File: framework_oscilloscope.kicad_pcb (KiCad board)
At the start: 4 copper layers, 26 x 44 mm, 83 parts, among them IC1 FT232HL-REEL, IC10 93LC56BT-I_OT, IC2 ICE40UP5K-SG48I, IC3 ADC08060CIMTX_NOPB, IC7 OPA356AIDBVR, IC8 TLV77312PDBVR, IC9 LM4040C20IDBZT, J1 BNC, P1 USB_C_Plug_USB2.0, U9 TPS62A02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

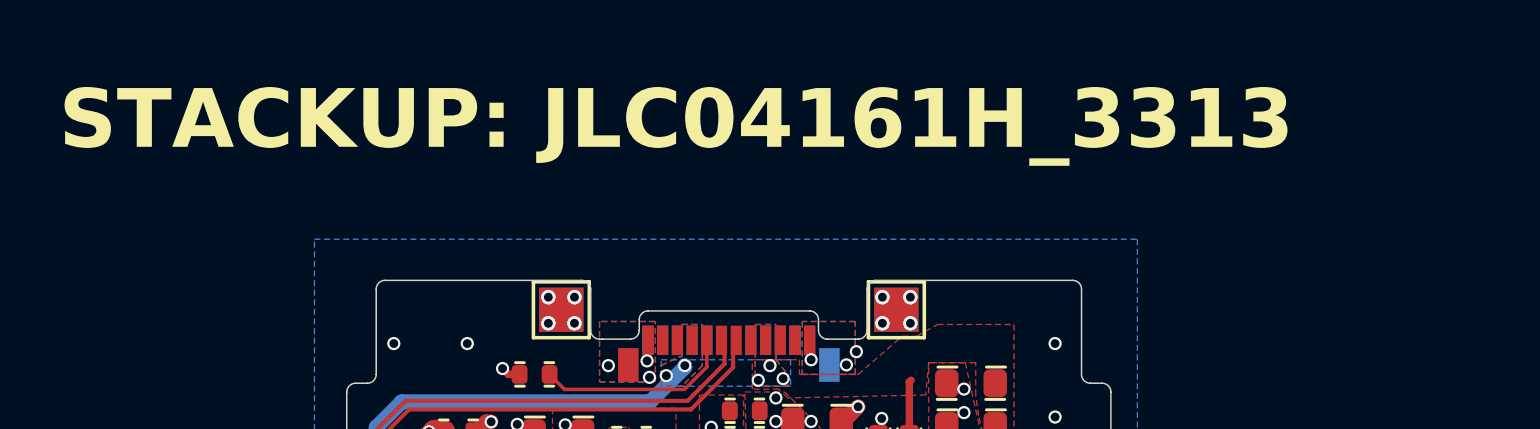
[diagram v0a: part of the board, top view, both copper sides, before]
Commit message: changed stackup name to a similar 0.8mm one
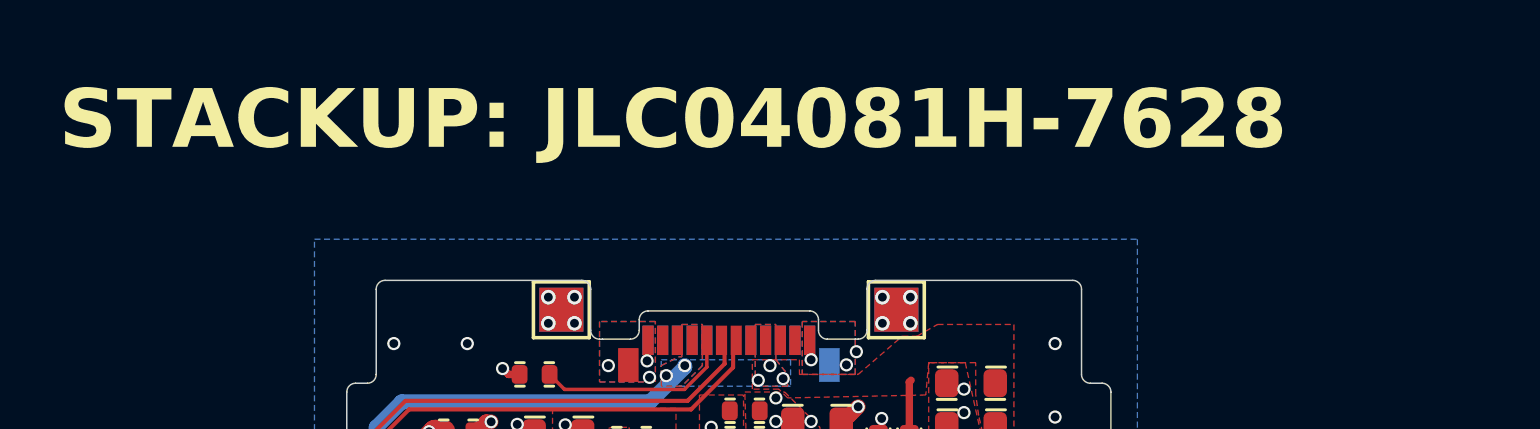
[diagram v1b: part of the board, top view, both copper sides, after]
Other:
- board text added: "STACKUP: JLC04081H-7628"
- board text removed: "STACKUP: JLC04161H_3313"
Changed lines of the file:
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@@
 		(layer "Edge.Cuts")
 	)
-	(gr_text "STACKUP: JLC04161H_3313"
+	(gr_text "STACKUP: JLC04081H-7628"
 		(at 45.45 31.725 0)
 		(layer "F.SilkS")

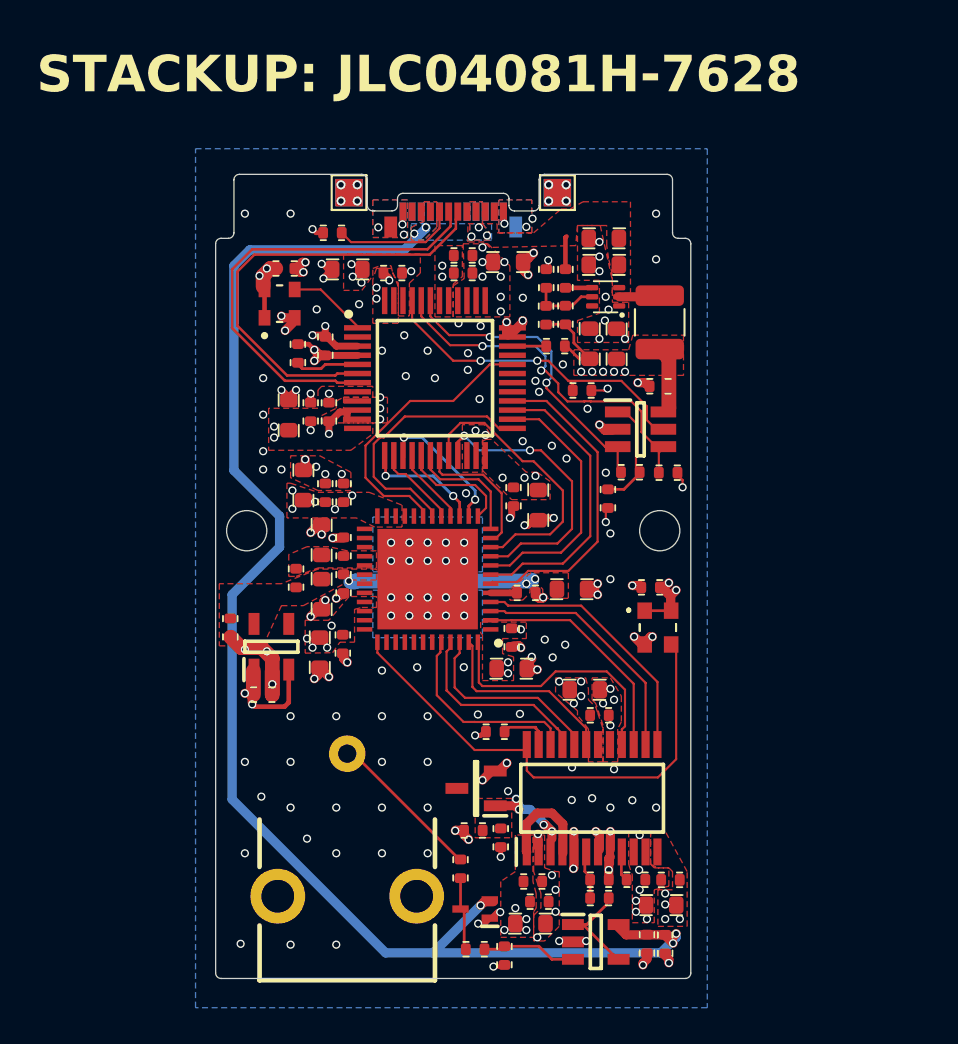
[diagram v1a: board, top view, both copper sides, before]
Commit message: fixed FT232-FPGA connections
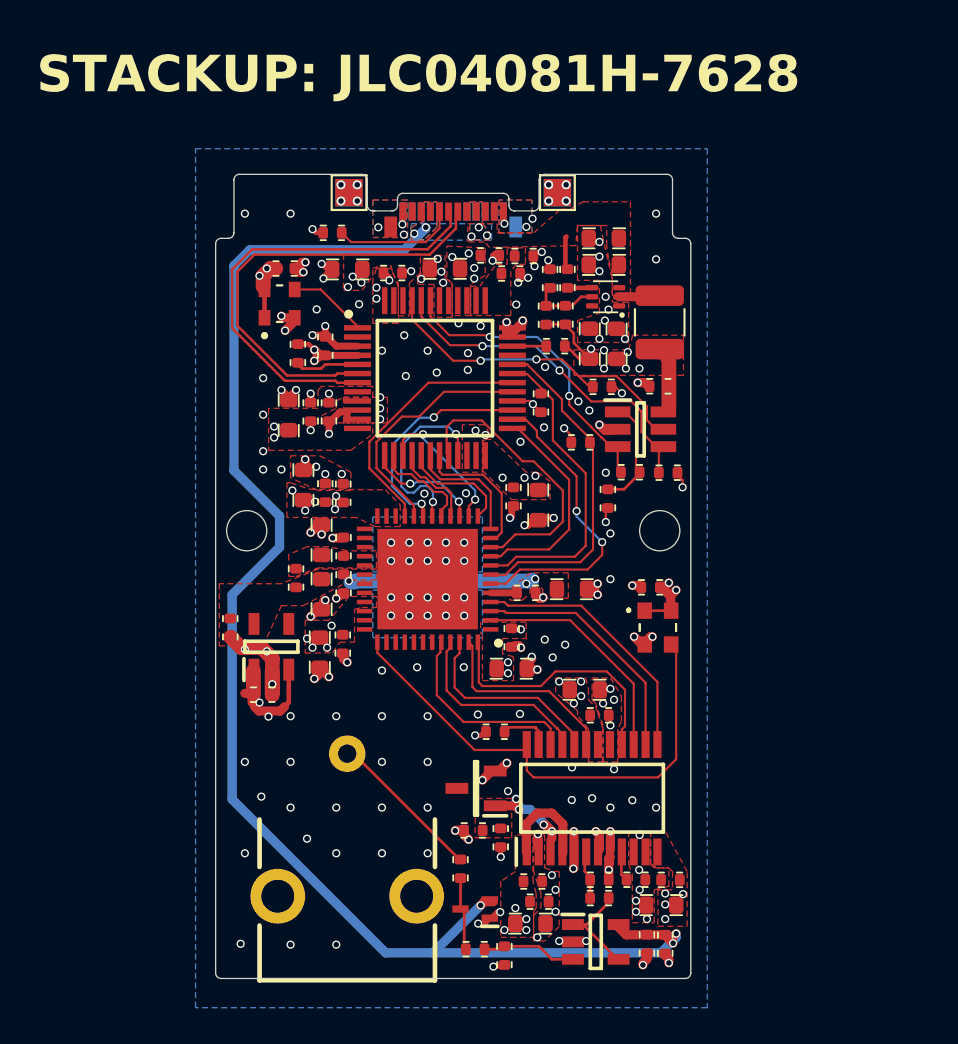
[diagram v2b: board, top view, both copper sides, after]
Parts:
- removed C28: 1uF, framework_oscilloscope:0402_1005Metric_CAP
- added C48: 100nF, framework_oscilloscope:0402_1005Metric_CAP, F.Cu at (72.1, 40.5)
- added C49: 100nF, framework_oscilloscope:0402_1005Metric_CAP, F.Cu at (71.4, 41.5)
- added R18: 10kR, framework_oscilloscope:0402_1005Metric, F.Cu at (75.2, 50.7)
- added R19: 10kR, framework_oscilloscope:0402_1005Metric, F.Cu at (73.0, 48.5)
- moved C36 3.47 mm to (67.8, 41.2), turned to 180 degrees
- moved C29 1.75 mm to (70.3, 40.5), turned to 0 degrees
- moved R17 1.12 mm to (76.4, 47.6)
- moved R6 0.21 mm to (73.6, 41.7)
- moved R7 0.11 mm to (74.5, 41.7)
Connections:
- IC1 pad 21: /FT232H_WR -> /FT232H_RXF
- IC1 pad 26: /CRESET_B -> /FT232H_RD
- IC1 pad 27: /CDONE -> /FT232H_WR
- IC1 pad 28: /ACBUS4 -> +3V3
- IC1 pad 29: unconnected-(IC1A-ACBUS5-Pad29) -> /FT232H_CLKOUT
- IC1 pad 30: unconnected-(IC1A-ACBUS6-Pad30) -> /FT232H_OE
- IC1 pad 31: unconnected-(IC1A-ACBUS7-Pad31) -> /CRESET_B
- IC1 pad 32: /FT232H_CLKOUT -> /CDONE
- IC1 pad 37: +3V3 -> +1V8_OUT
- IC1 pad 38: +3V3 -> +1V8_OUT
- IC2 pad 18: /FT232H_TXE -> /FT232H_RXF
- IC2 pad 19: /FT232H_CLKOUT -> /FT232H_WR
- IC2 pad 20: unconnected-(IC2-IOB_25B_G3-Pad20) -> /FT232H_CLKOUT
- IC2 pad 21: unconnected-(IC2-IOB_23B-Pad21) -> /FT232H_OE
- IC2 pad 6: /ACBUS4 -> /FT232H_RD
- IC2 pad 9: /FT232H_WR -> /FT232H_TXE
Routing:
- net /ACBUS4: track 17.5 -> 0.00 mm
- net /FT232H_RD: track 0.00 -> 16.6 mm, vias 0 -> 2
- net /FT232H_OE: track 0.00 -> 14.0 mm
- net /FT232H_RXF: track 0.00 -> 10.5 mm, vias 0 -> 2
- net +3V3: track 32.8 -> 36.4 mm
- net /FT232H_WR: track 15.8 -> 12.4 mm
- net /CRESET_B: track 14.3 -> 17.4 mm
- net /FT232H_TXE: track 14.5 -> 11.9 mm
- net /CDONE: track 16.0 -> 18.5 mm
- net /FT232H_CLKOUT: track 15.9 -> 13.7 mm
- net GND: track 49.2 -> 50.5 mm, vias 202 -> 205
- net Net-(IC10-CLK): track 20.3 -> 19.2 mm
- net /SPI_SI: track 4.62 -> 5.49 mm
- net /SPI_SS: track 4.18 -> 4.70 mm
- net /ADBUS7: track 15.4 -> 15.9 mm
- added copper zone on F.Cu, net +1V8_OUT

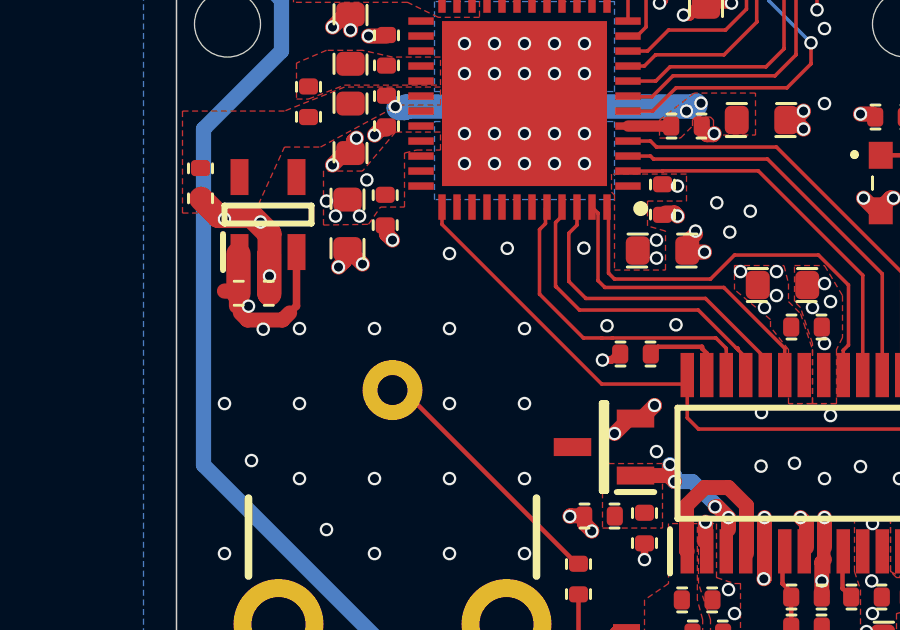
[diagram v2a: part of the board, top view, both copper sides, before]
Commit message: added part numbers for passives
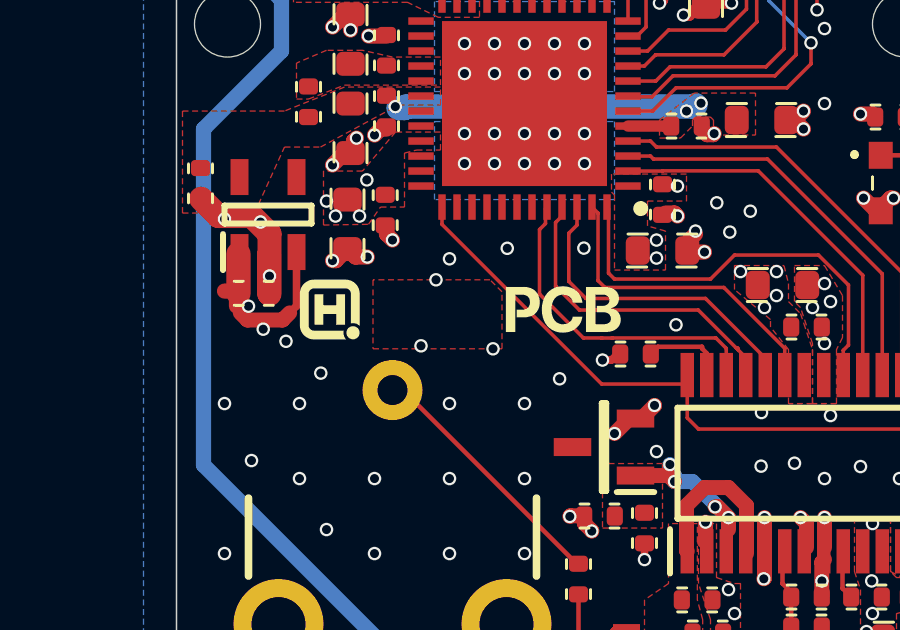
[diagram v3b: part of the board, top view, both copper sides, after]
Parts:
- added LOGO1: ~, amemb-Symbol:NextPCB, F.Cu at (64.7, 65.0)
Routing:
- net GND: vias 205 -> 206

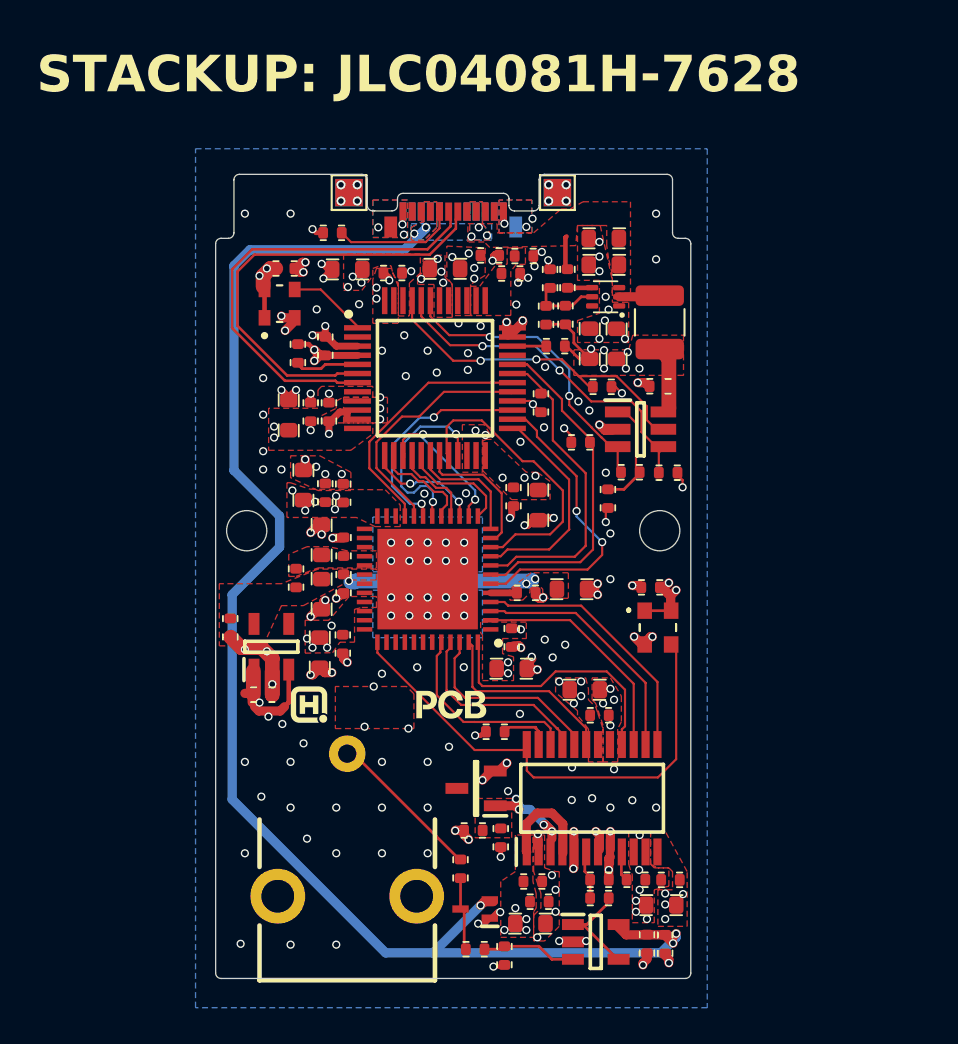
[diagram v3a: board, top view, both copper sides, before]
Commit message: improved dfm
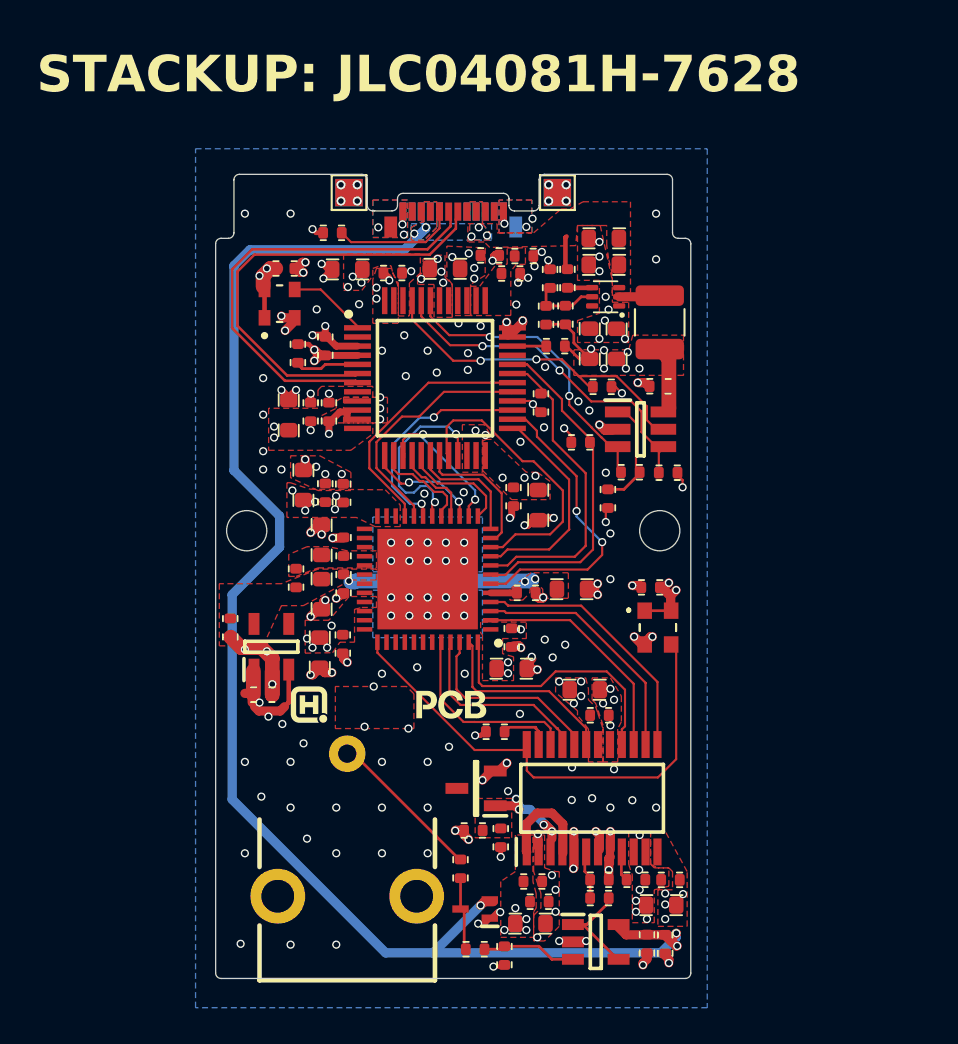
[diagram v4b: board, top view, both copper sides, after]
